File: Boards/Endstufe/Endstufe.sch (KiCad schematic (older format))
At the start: 56 parts, among them J1 HV In, J2 Relais, J3 NF_In, J4 Trafo, K1 G6E, P4 6V3_AC, P5 Trafo_GK, P6 6V3_DC, P7 VSup1, P8 Bias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

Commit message: Layout changes, Supply connector changes, Mounting holes
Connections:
- net +240V: now also J1.4 (Pin_4); no longer J1.2 (Pin_2)
- net +300V: now also J1.6 (Pin_6); no longer J1.4 (Pin_4)
- net -120V: now also J1.2 (Pin_2); no longer J1.6 (Pin_6)
- net -60V: now also J1.1 (Pin_1)
- net GND: no longer J1.1 (Pin_1)
- net UG_1: now also P8.2 (P2), R8.2; no longer C5.1, R2.1, R7.2, R8.1
- net UG_2: now also P8.5 (P5), R14.2; no longer C9.2, R14.1, R17.1, R21.2
- new net: C14.1, C5.1, R2.1, R7.2, R8.1
- new net: C15.1, C9.2, R14.1, R17.1, R21.2
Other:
- note added: "ECC83 Phasenumkehr / ECC82 Treiberstufe"
- note added: "Gitter-\nVorspannung"
- note added: "Roederstein \nMKT 1813\n400 V DC"
- note added: "Roederstein\nMKT1813\n400 V DC"
- note removed: "ECC83 Vorstufe"
- moved on the sheet: C14, C15, C5, C9, P6, R14, R17, R2, R21, R7, R8, U1C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

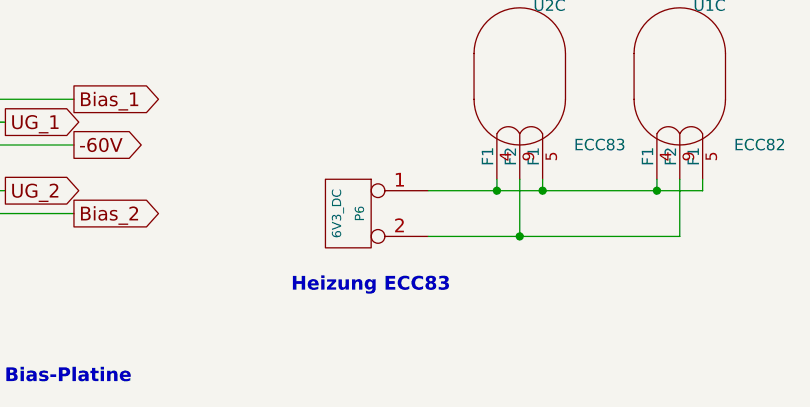
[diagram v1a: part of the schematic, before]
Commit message: Adjusted Silkscreen
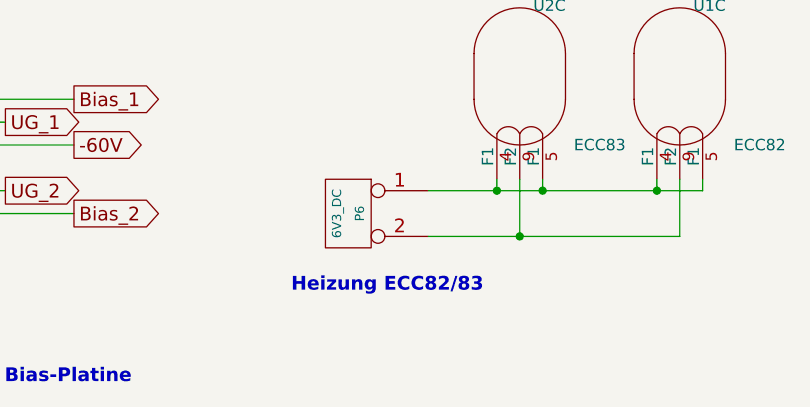
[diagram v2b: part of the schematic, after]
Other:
- note added: "Heizung ECC82/83"
- note removed: "Heizung ECC83"
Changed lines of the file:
@@
 	5250 7000 5650 7000
 Text Notes 4650 7250 0    60   ~ 12
-Heizung ECC83
+Heizung ECC82/83
 Text Notes 1500 1850 0    60   ~ 0
 Roederstein MKT 1813\n400 V DC

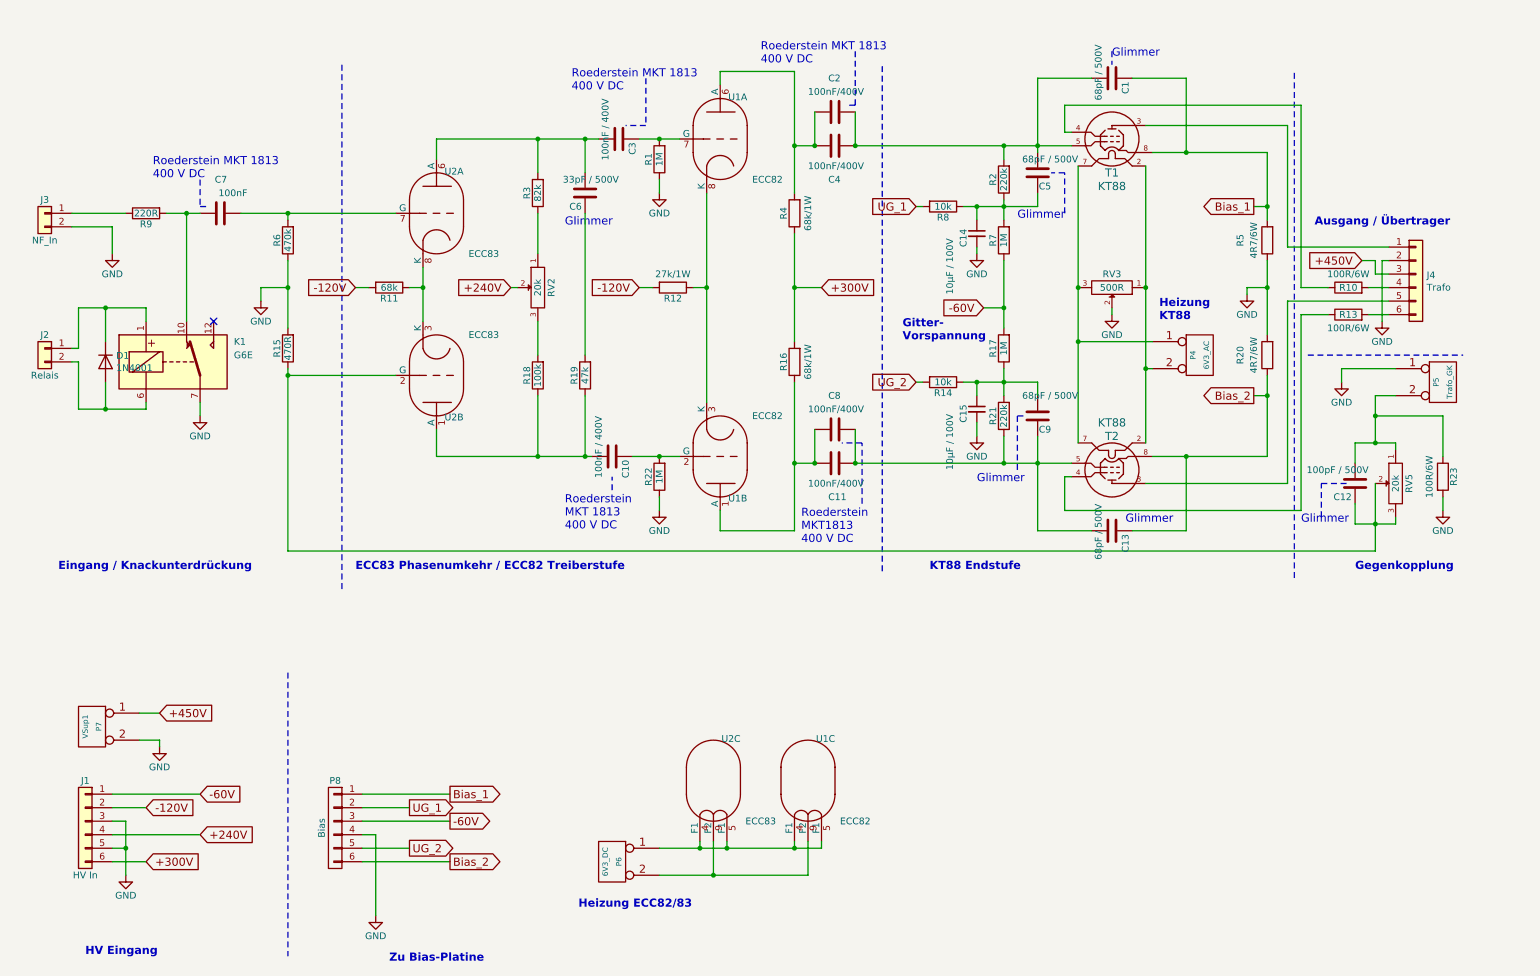
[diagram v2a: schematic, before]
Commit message: Added Mounting holes, Moved -60V Divider to HV Board, eliminated +450V Connector and Feedback Connector on Amp Board
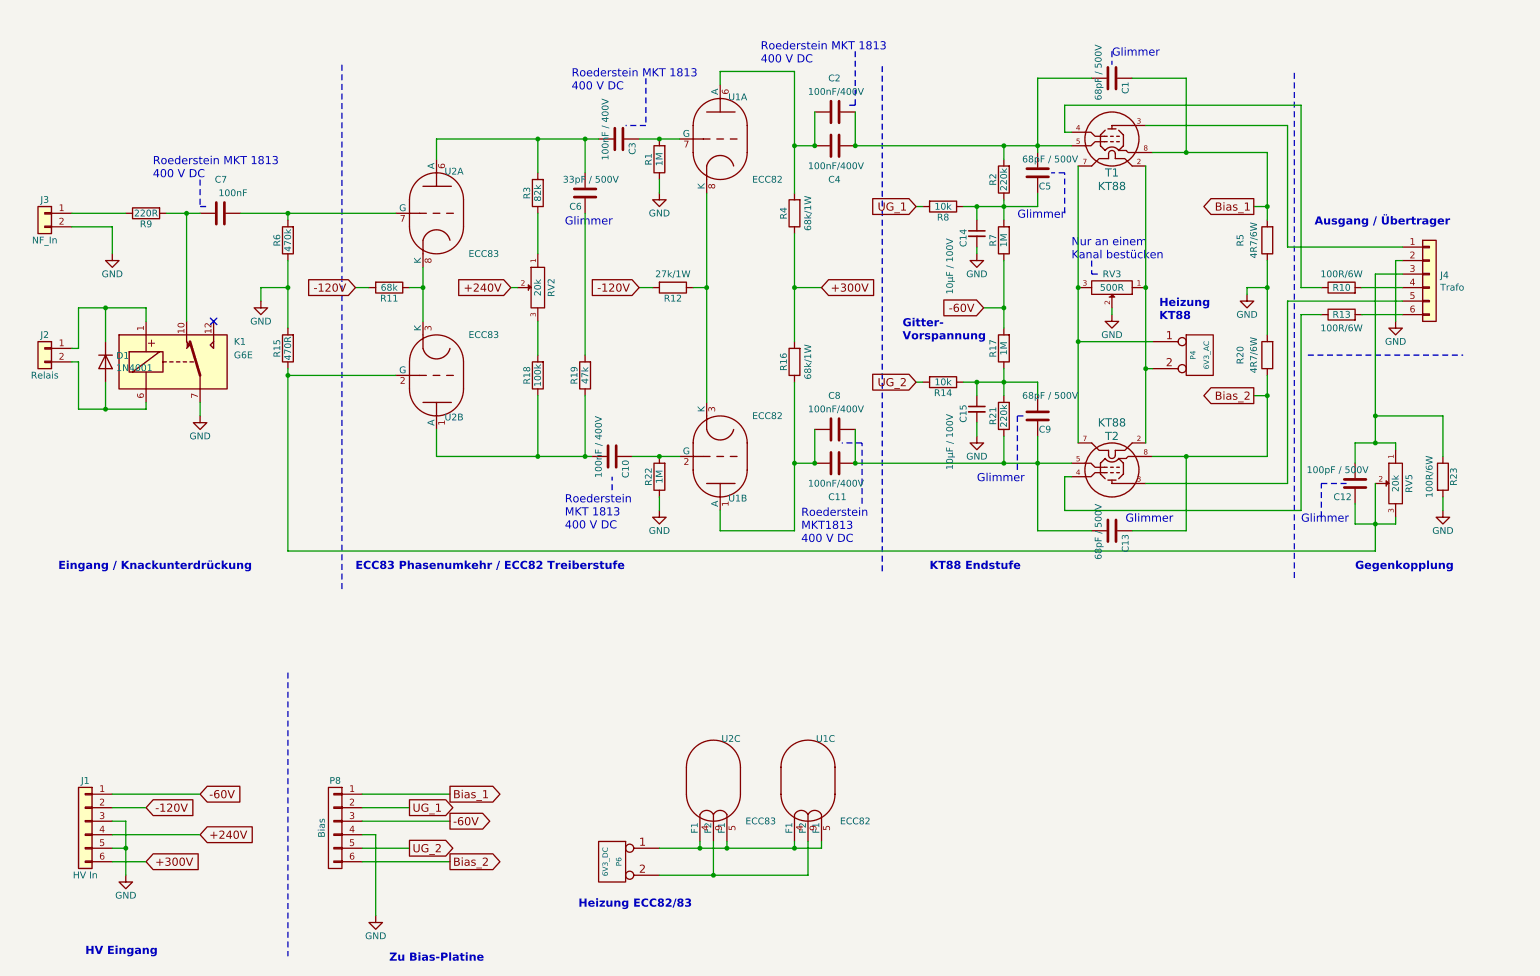
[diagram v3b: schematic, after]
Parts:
- removed P5: Trafo_GK, Connector_TE-Connectivity:TE_MATE-N-LOK_1-770866-x_1x02_P4.14mm_Vertical, symbol Endstufe-rescue:CONN_2
- removed P7: VSup1, Connector_TE-Connectivity:TE_MATE-N-LOK_1-770866-x_1x02_P4.14mm_Vertical, symbol Endstufe-rescue:CONN_2
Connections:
- net +450V is gone; now on an unnamed net: J4.3 (Pin_3)
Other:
- note added: "Nur an einem \nKanal bestücken"
- moved on the sheet: J4, R10, R13
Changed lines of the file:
@@
 EESchema Schematic File Version 4
-LIBS:Endstufe-cache
 EELAYER 30 0
 EELAYER END
@@
 $EndComp
 $Comp
-L Endstufe-rescue:CONN_2 P5
-U 1 1 55CA233F
-P 11050 3350
-F 0 "P5" V 11000 3350 40  0000 C CNN
-F 1 "Trafo_GK" V 11100 3350 40  0000 C CNN
-F 2 "Connector_TE-Connectivity:TE_MATE-N-LOK_1-770866-x_1x02_P4.14mm_Vertical" H 11050 3350 60  0001 C CNN
-F 3 "" H 11050 3350 60  0000 C CNN
-	1    11050 3350
-	1    0    0    -1
-$EndComp
-$Comp
 L Endstufe-rescue:POT-RESCUE-Endstufe RV5
 U 1 1 55CA2532
@@
 $EndComp
 $Comp
-L Endstufe-rescue:GND #PWR06
-U 1 1 55CA27EB
-P 10300 3350
-F 0 "#PWR06" H 10300 3100 50  0001 C CNN
-F 1 "GND" H 10300 3200 50  0000 C CNN
-F 2 "" H 10300 3350 60  0000 C CNN
-F 3 "" H 10300 3350 60  0000 C CNN
-	1    10300 3350
-	1    0    0    -1
-$EndComp
-$Comp
 L Endstufe-rescue:R R10
 U 1 1 55CB6557
-P 10350 2650
-F 0 "R10" V 10350 2650 50  0000 C CNN
-F 1 "100R/6W" V 10450 2650 50  0000 C CNN
-F 2 "Resistor_THT:R_Axial_Power_L25.0mm_W9.0mm_P30.48mm" V 10280 2650 30  0001 C CNN
-F 3 "" H 10350 2650 30  0000 C CNN
-	1    10350 2650
+P 10300 2650
+F 0 "R10" V 10300 2650 50  0000 C CNN
+F 1 "100R/6W" V 10400 2650 50  0000 C CNN
+F 2 "Resistor_THT:R_Axial_Power_L25.0mm_W9.0mm_P30.48mm" V 10230 2650 30  0001 C CNN
+F 3 "" H 10300 2650 30  0000 C CNN
+	1    10300 2650
 	0    -1   -1   0
 $EndComp
@@
 L Endstufe-rescue:R R13
 U 1 1 55CB6AF7
-P 10350 2850
-F 0 "R13" V 10350 2850 50  0000 C CNN
-F 1 "100R/6W" V 10250 2850 50  0000 C CNN
-F 2 "Resistor_THT:R_Axial_Power_L25.0mm_W9.0mm_P30.48mm" V 10280 2850 30  0001 C CNN
-F 3 "" H 10350 2850 30  0000 C CNN
-	1    10350 2850
+P 10300 2850
+F 0 "R13" V 10300 2850 50  0000 C CNN
+F 1 "100R/6W" V 10200 2850 50  0000 C CNN
+F 2 "Resistor_THT:R_Axial_Power_L25.0mm_W9.0mm_P30.48mm" V 10230 2850 30  0001 C CNN
+F 3 "" H 10300 2850 30  0000 C CNN
+	1    10300 2850
 	0    -1   -1   0
 $EndComp
-Text GLabel 10450 2450 0    60   Input ~ 0
-+450V
 $Comp
 L Endstufe-rescue:GND #PWR07
@@
 Text Notes 6300 4550 0    60   ~ 0
 Roederstein\nMKT1813\n400 V DC
-$Comp
-L Endstufe-rescue:CONN_2 P7
-U 1 1 56BBDA5D
-P 1050 5900
-F 0 "P7" V 1000 5900 40  0000 C CNN
-F 1 "VSup1" V 1100 5900 40  0000 C CNN
-F 2 "Connector_TE-Connectivity:TE_MATE-N-LOK_1-770866-x_1x02_P4.14mm_Vertical" H 1050 5900 60  0001 C CNN
-F 3 "" H 1050 5900 60  0000 C CNN
-	1    1050 5900
-	-1   0    0    -1
-$EndComp
-$Comp
-L Endstufe-rescue:GND #PWR010
-U 1 1 56BBED46
-P 1550 6050
-F 0 "#PWR010" H 1550 5800 50  0001 C CNN
-F 1 "GND" H 1550 5900 50  0000 C CNN
-F 2 "" H 1550 6050 60  0000 C CNN
-F 3 "" H 1550 6050 60  0000 C CNN
-	1    1550 6050
-	1    0    0    -1
-$EndComp
-Text GLabel 1550 5800 2    60   Input ~ 0
-+450V
 Wire Wire Line
 	3500 2500 3500 2650
@@
 Connection ~ 10550 4400
 Wire Wire Line
-	10300 3250 10300 3350
-Wire Wire Line
 	10550 4600 10550 4400
 Wire Wire Line
 	10700 3800 10700 3850
-Wire Wire Line
-	10300 3250 10700 3250
 Wire Wire Line
 	10400 3950 10400 3800
@@
 	8850 4100 9900 4100
 Wire Wire Line
-	10000 2650 10200 2650
-Wire Wire Line
-	10700 3450 10550 3450
-Wire Wire Line
-	10550 3450 10550 3600
+	10000 2650 10150 2650
 Connection ~ 10550 3800
 Wire Wire Line
@@
 Wire Notes Line
 	2900 1000 2900 4900
-Wire Wire Line
-	1400 5800 1550 5800
-Wire Wire Line
-	1400 6000 1550 6000
-Wire Wire Line
-	1550 6000 1550 6050
 $Comp
 L Endstufe-rescue:GND #PWR011
@@
 L Connector_Generic:Conn_01x06 J4
 U 1 1 5CC18566
-P 10850 2550
-F 0 "J4" H 10930 2542 50  0000 L CNN
-F 1 "Trafo" H 10930 2451 50  0000 L CNN
-F 2 "Connector_TE-Connectivity:TE_MATE-N-LOK_1-770875-x_2x03_P4.14mm_Vertical" H 10850 2550 50  0001 C CNN
-F 3 "~" H 10850 2550 50  0001 C CNN
-	1    10850 2550
+P 10950 2550
+F 0 "J4" H 11030 2542 50  0000 L CNN
+F 1 "Trafo" H 11030 2451 50  0000 L CNN
+F 2 "Connector_TE-Connectivity:TE_MATE-N-LOK_1-770875-x_2x03_P4.14mm_Vertical" H 10950 2550 50  0001 C CNN
+F 3 "~" H 10950 2550 50  0001 C CNN
+	1    10950 2550
 	1    0    0    -1
 $EndComp
@@
 	9900 1450 9900 2350
 Wire Wire Line
-	10650 2350 9900 2350
-Wire Wire Line
-	10500 2650 10650 2650
+	10750 2350 9900 2350
+Wire Wire Line
+	10450 2650 10750 2650
 $Comp
 L Endstufe-rescue:GND #PWR0101
 U 1 1 5CCAF2A5
-P 10600 2900
-F 0 "#PWR0101" H 10600 2650 50  0001 C CNN
-F 1 "GND" H 10600 2750 50  0000 C CNN
-F 2 "" H 10600 2900 60  0000 C CNN
-F 3 "" H 10600 2900 60  0000 C CNN
-	1    10600 2900
-	1    0    0    -1
-$EndComp
-Wire Wire Line
-	10600 2450 10650 2450
-Wire Wire Line
-	10600 2450 10600 2900
-Wire Wire Line
-	10650 2850 10500 2850
-Wire Wire Line
-	10200 2850 10000 2850
-Wire Wire Line
-	10650 2750 9900 2750
+P 10700 2900
+F 0 "#PWR0101" H 10700 2650 50  0001 C CNN
+F 1 "GND" H 10700 2750 50  0000 C CNN
+F 2 "" H 10700 2900 60  0000 C CNN
+F 3 "" H 10700 2900 60  0000 C CNN
+	1    10700 2900
+	1    0    0    -1
+$EndComp
+Wire Wire Line
+	10700 2450 10750 2450
+Wire Wire Line
+	10700 2450 10700 2900
+Wire Wire Line
+	10750 2850 10450 2850
+Wire Wire Line
+	10150 2850 10000 2850
+Wire Wire Line
+	10750 2750 9900 2750
 Wire Wire Line
 	9900 2750 9900 4100
-Wire Wire Line
-	10450 2450 10550 2450
-Wire Wire Line
-	10550 2450 10550 2550
-Wire Wire Line
-	10550 2550 10650 2550
 Wire Notes Line
 	10150 4350 10150 4100
@@
 Text Notes 7050 3050 0    60   ~ 12
 Gitter-\nVorspannung
+Text Notes 8300 2450 0    60   ~ 0
+Nur an einem \nKanal bestücken
+Wire Notes Line
+	8450 2450 8450 2550
+Wire Notes Line
+	8450 2550 8500 2550
+Wire Wire Line
+	10550 2550 10750 2550
+Wire Wire Line
+	10550 2550 10550 3600
 $EndSCHEMATC
